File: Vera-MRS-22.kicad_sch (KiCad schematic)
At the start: 18 parts, among them J4 Screw_Terminal_01x10, Q1 BC337, Q2 BC337, U2 NUCLEO-F303K8

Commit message: Finished RevB and sent for manufature
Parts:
- removed U2: NUCLEO-F303K8, Vera-MRS-21:NUCLEO_32, symbol Vera-MRS-21:NUCLEO-F303K8
- added J1: 2x16_2.54P_pin_header, Connector_PinHeader_2.54mm:PinHeader_2x16_P2.54mm_Vertical, symbol Vera-MRS-21:2x16_2.54P_pin_header
- added R6: 10k, Resistor_THT:R_Axial_DIN0207_L6.3mm_D2.5mm_P10.16mm_Horizontal, symbol Motorrumsstyrning-rescue:R_Small-Device
- added R7: 4k2, Resistor_THT:R_Axial_DIN0207_L6.3mm_D2.5mm_P10.16mm_Horizontal, symbol Motorrumsstyrning-rescue:R_Small-Device
- added U2: NUCLEO-G031K8 Physical, Vera-MRS-21:NUCLEO_32, symbol Vera-MRS-21:NUCLEO-G031K8 Physical
- C1: value (none) -> 0.33u; footprint (none) -> Capacitor_SMD:C_1206_3216Metric_Pad1.33x1.80mm_HandSolder
- C2: value (none) -> 0.1u; footprint (none) -> Capacitor_SMD:C_1206_3216Metric_Pad1.33x1.80mm_HandSolder
- R1: renamed from R4; value (none) -> 10k; footprint (none) -> Resistor_THT:R_Axial_DIN0207_L6.3mm_D2.5mm_P10.16mm_Horizontal
- R2: renamed from R5; value (none) -> 4k2; footprint (none) -> Resistor_THT:R_Axial_DIN0207_L6.3mm_D2.5mm_P10.16mm_Horizontal
- R3: renamed from R1; value 3k6 -> 10k
- R4: renamed from R2; value 10k -> 4k2
- R5: renamed from R3; value (none) -> 1k; footprint (none) -> Resistor_THT:R_Axial_DIN0207_L6.3mm_D2.5mm_P10.16mm_Horizontal
- U1: value (none) -> LD1117V50; footprint (none) -> Package_TO_SOT_THT:TO-220-3_Horizontal_TabDown
- renumbered J4 to J2, JP2 to JP1, JP1 to JP2, Q2 to Q1, Q1 to Q2
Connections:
- net GNDS is gone; now on net GND: J2.10 (Pin_10), R2.2, R4.2
- net Injector_Out is gone; now on net Start_Relay_GND: J2.7 (Pin_7)
- net Start_Relay_Gnd is gone; now on net Injector-: J2.8 (Pin_8)
- net +12V: now also J1.32 (B16)
- net +5V: now also J1.1 (A1), U2.CN4_1 (VIN)
- net Injector_Enable: now also J1.29 (A15), U2.CN4_15 (PB3)
- net RPM: now also J1.12 (B6), U2.CN3_6 (PB1)
- net RPM_Tach: now also J2.4 (Pin_4); no longer J2.5 (Pin_5)
- net Start_Enable: now also J1.23 (A12), U2.CN4_12 (PA0)
- net USART1_RX: now also J1.4 (B2), U2.CN3_2 (PB7)
- net USART1_TX: now also J1.2 (B1), U2.CN3_1 (PB6)
- net VEL: now also J1.9 (A5), U2.CN4_5 (PA7)
- net VEL_Tach: now also J2.5 (Pin_5); no longer J2.4 (Pin_4)
- net GNDPWR renamed GND
- net GND: now also J1.3 (A2), J1.31 (A16), J1.8 (B4), R7.2, U2.CN3_4 (GND), U2.CN4_2 (GND); no longer J2.9 (Pin_9)
- net Injector_IN renamed Injector+
- net Injector+: now also J2.9 (Pin_9); no longer J2.6 (Pin_6)
- net Injector_OUT renamed Injector-
- new net: J1.20 (B10), U2.CN3_10 (PB2)
- new net: J1.22 (B11), U2.CN3_11 (PB8)
- new net: J1.24 (B12), U2.CN3_12 (PA8)
- new net: J1.26 (B13), U2.CN3_13 (PB9)
- new net: J1.28 (B14), U2.CN3_14 (PB5)
- new net: J1.30 (B15), U2.CN3_15 (PB4)
- new net: J1.6 (B3), U2.CN3_3 (~{RST})
- new net: J1.10 (B5), U2.CN3_5 (PA15)
- new net: J1.14 (B7), U2.CN3_7 (PA10)
- new net: J1.16 (B8), U2.CN3_8 (PA9)
- new net: J1.18 (B9), U2.CN3_9 (PB0)
- new net: J1.19 (A10), U2.CN4_10 (PA4)
- new net: J1.21 (A11), U2.CN4_11 (PA1)
- new net: J1.25 (A13), U2.CN4_13 (AREF)
- new net: J1.27 (A14), U2.CN4_14 (+3V3)
- new net: J1.5 (A3), U2.CN4_3 (~{RST})
- new net: J1.7 (A4), U2.CN4_4 (+5V)
- new net: J1.11 (A6), U2.CN4_6 (PA6)
- new net: J1.13 (A7), U2.CN4_7 (PA11)
- new net: J1.15 (A8), U2.CN4_8 (PA12)
- new net Deadmans: J1.17 (A9), R6.2, R7.1, U2.CN4_9 (PA5)
- new net Deadmans_12V: J2.6 (Pin_6), R6.1
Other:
- moved on the sheet: C1, C2, H1, H2, H3, H4, J2, JP1, JP2, Q1, Q2, R1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

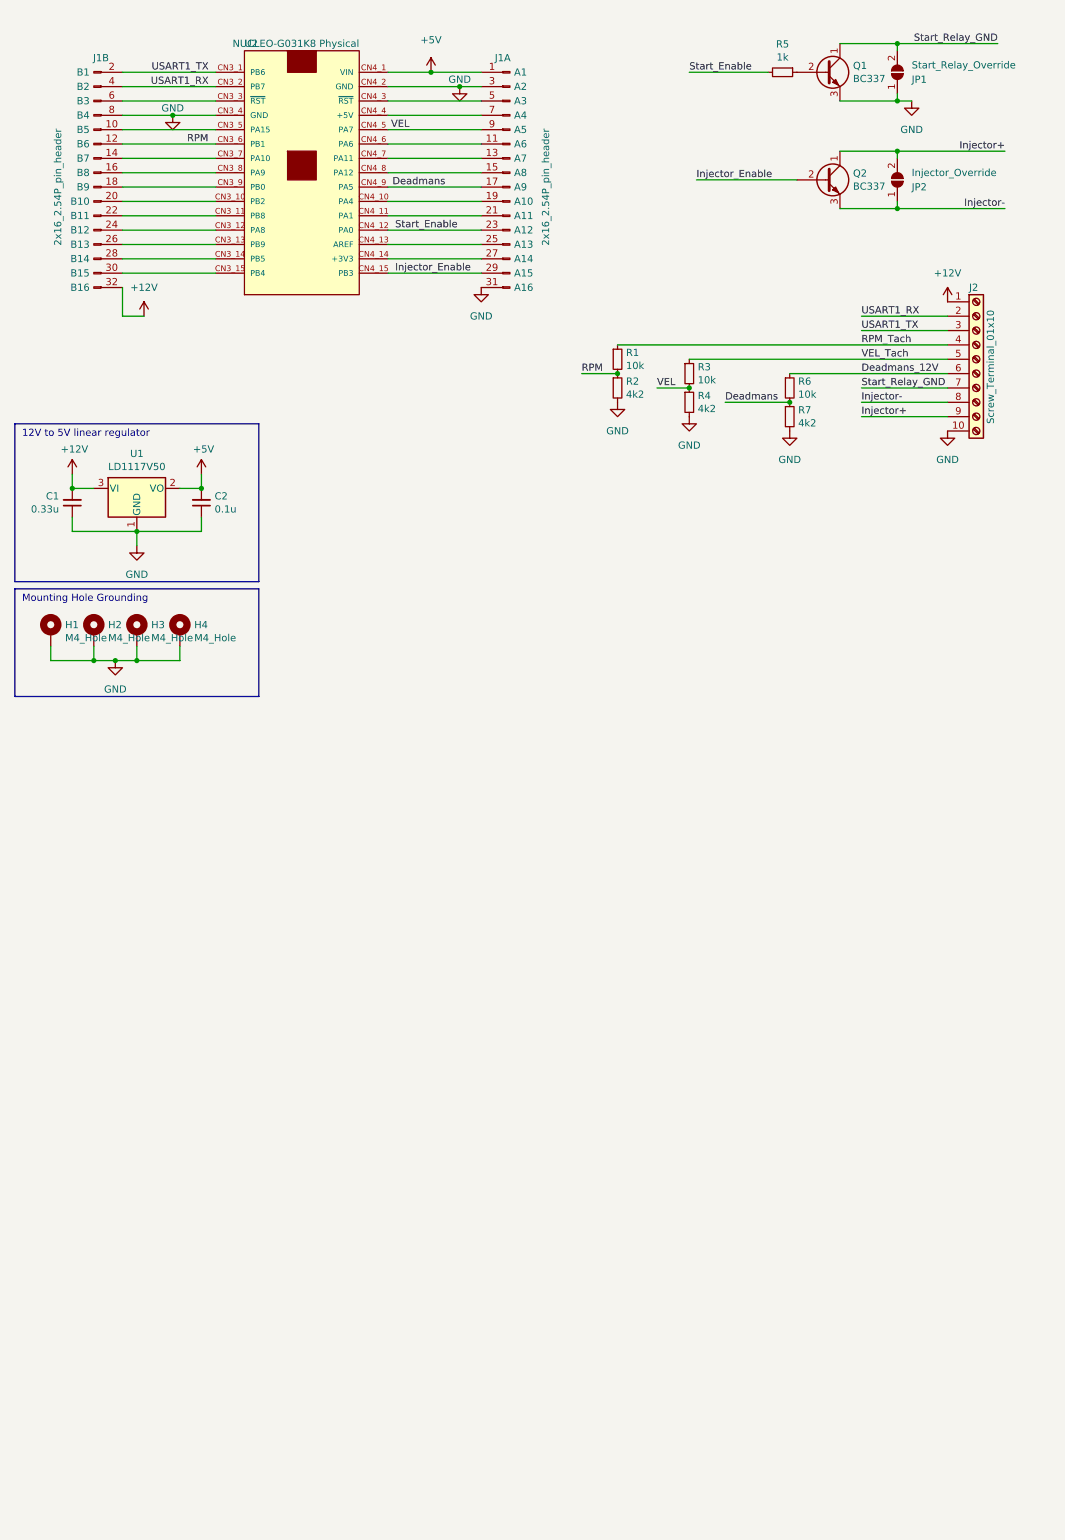
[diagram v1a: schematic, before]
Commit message: Rev.C
Added LEDs
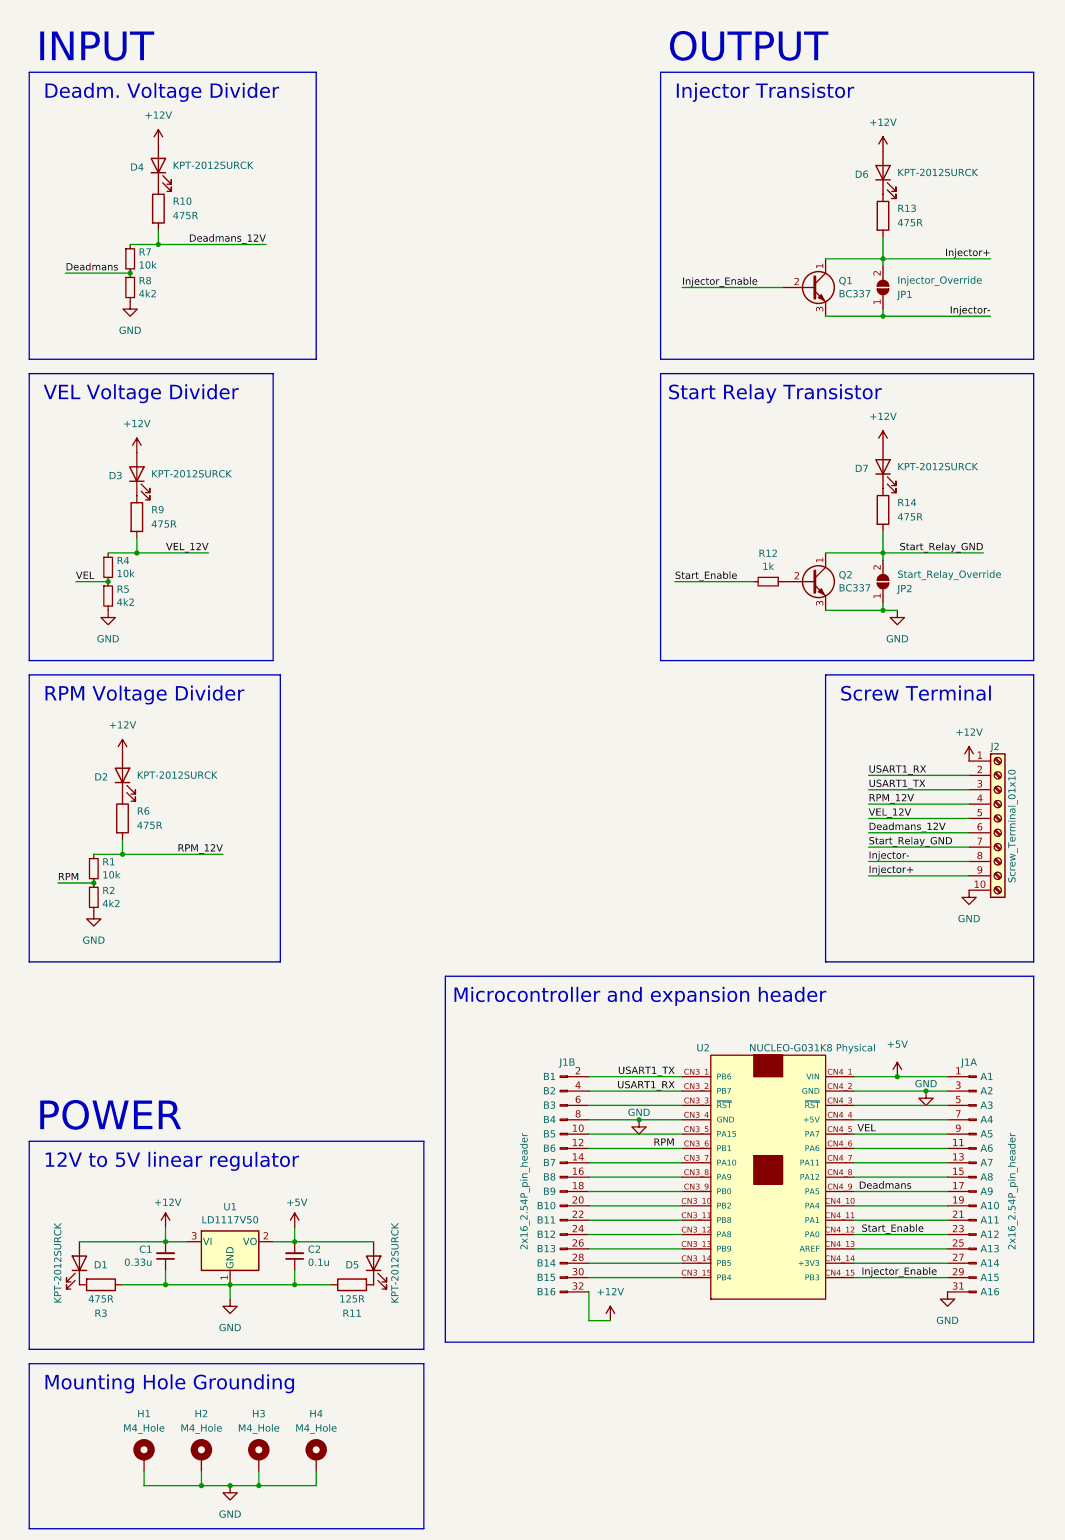
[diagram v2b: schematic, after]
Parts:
- added D1, D2, D3, D4, D5, D6, D7: KPT-2012SURCK, LED_SMD:LED_0805_2012Metric_Pad1.15x1.40mm_HandSolder, symbol Device:LED
- added R10, R13, R14, R3, R6, R9: 475R, Resistor_SMD:R_1206_3216Metric_Pad1.30x1.75mm_HandSolder, symbol Device:R
- added R11: 125R, Resistor_SMD:R_1206_3216Metric_Pad1.30x1.75mm_HandSolder, symbol Device:R
- renumbered JP2 to JP1, JP1 to JP2, Q2 to Q1, Q1 to Q2, R5 to R12, R3 to R4, R4 to R5, R6 to R7, R7 to R8
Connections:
- net +12V: now also D1.2 (A), D2.2 (A), D3.2 (A), D4.2 (A), D6.2 (A), D7.2 (A)
- net +5V: now also D5.2 (A)
- net Deadmans_12V: now also R10.2
- net GND: now also R11.1, R3.1
- net Injector+: now also R13.2
- net Start_Relay_GND: now also R14.2
- net RPM_Tach renamed RPM_12V
- net RPM_12V: now also R6.2
- net VEL_Tach renamed VEL_12V
- net VEL_12V: now also R9.2
- new net: D1.1 (K), R3.2
- new net: D6.1 (K), R13.1
- new net: D5.1 (K), R11.2
- new net: D3.1 (K), R9.1
- new net: D2.1 (K), R6.1
- new net: D4.1 (K), R10.1
- new net: D7.1 (K), R14.1
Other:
- note added: "Deadm. Voltage Divider"
- note added: "INPUT"
- note added: "Injector Transistor"
- note added: "Microcontroller and expansion header"
- note added: "OUTPUT"
- note added: "POWER"
- note added: "RPM Voltage Divider"
- note added: "Screw Terminal"
- note added: "Start Relay Transistor"
- note added: "VEL Voltage Divider"
- moved on the sheet: C1, C2, H1, H2, H3, H4, J1A, J1B, J2, JP1, JP2, Q1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
